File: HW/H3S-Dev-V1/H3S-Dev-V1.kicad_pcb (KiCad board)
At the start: 2 copper layers, 85 x 56 mm, 17 parts, among them J1 USB_C_Receptacle_USB2.0_16P, J2 Conn_01x02_Socket, J3 Conn_Coaxial, Q1 DMP3099L, U1 Ai-Thinker-Ra-01, U2 LTC4054ES5-4.2, U4 ESP32-S3-WROOM-1

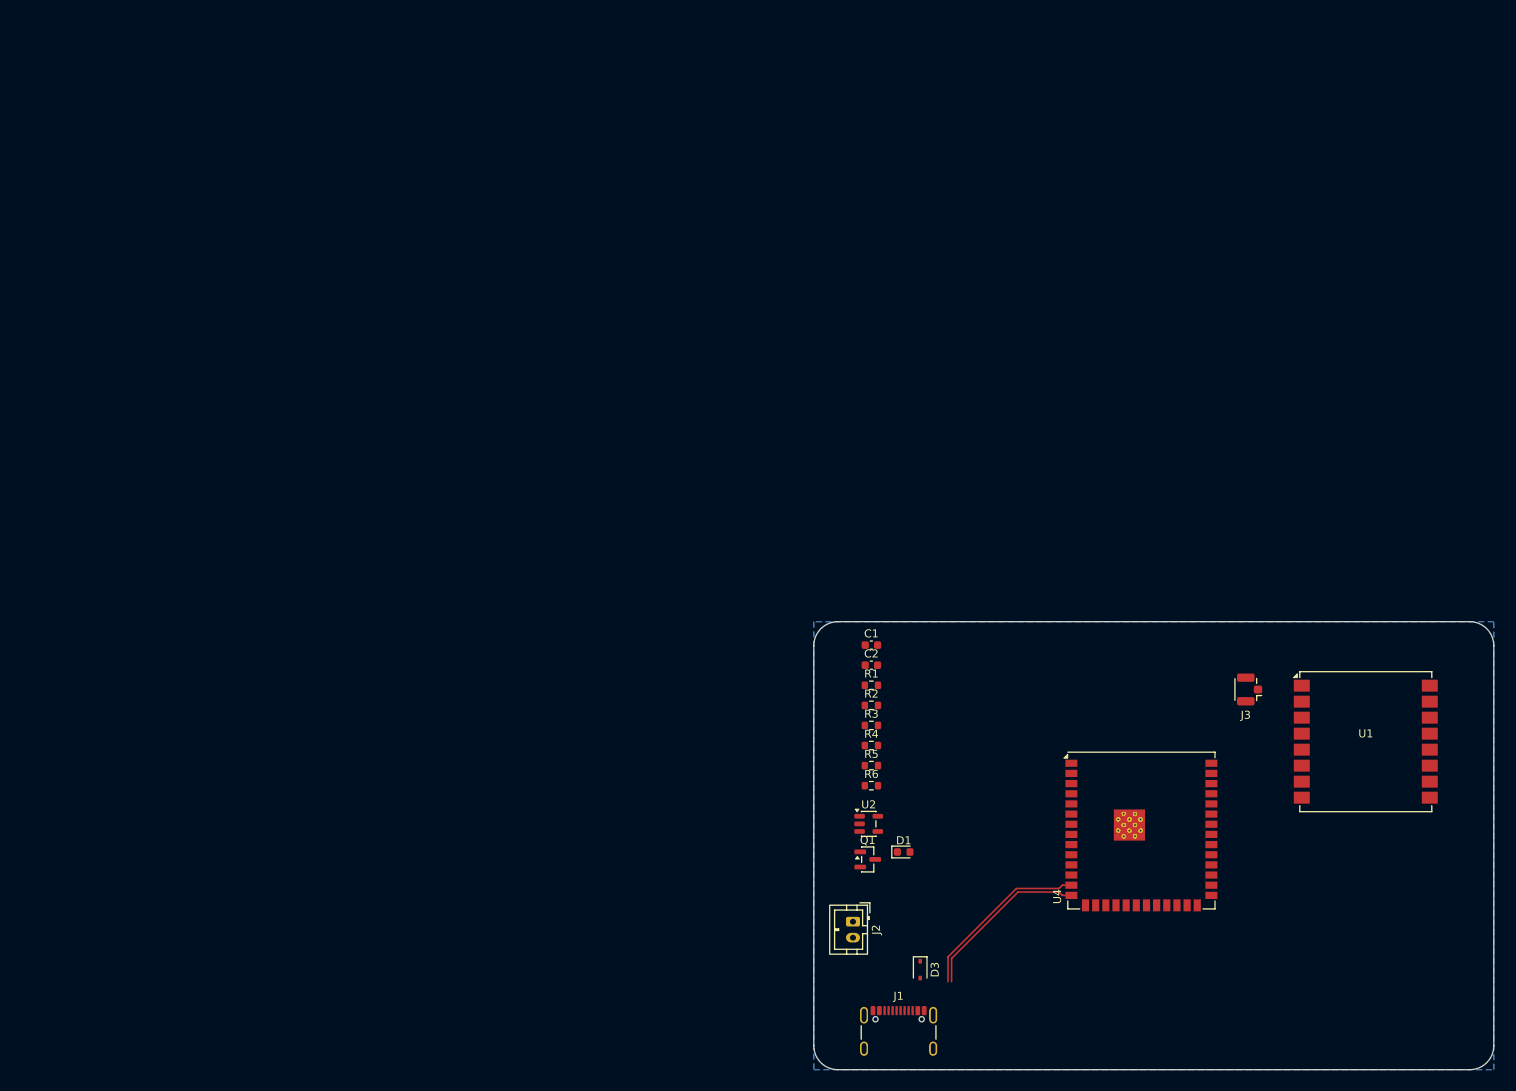
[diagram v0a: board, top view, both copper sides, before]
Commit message: Some components arranged
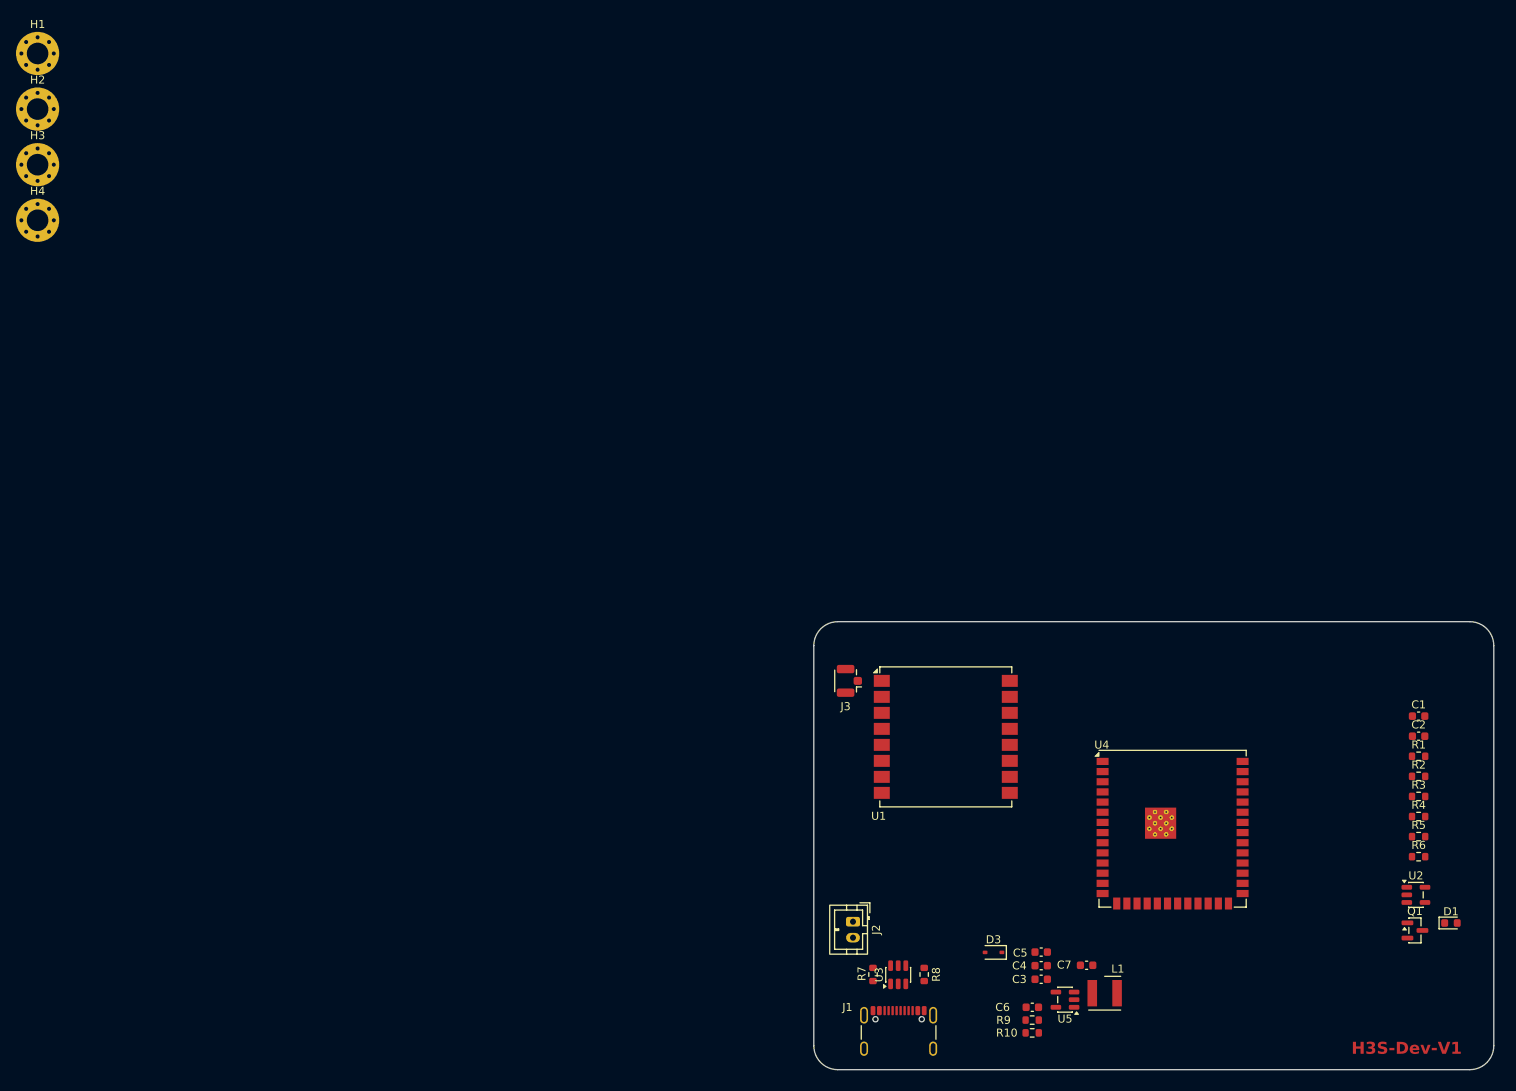
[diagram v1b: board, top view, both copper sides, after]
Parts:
- added C3: 100n, Capacitor_SMD:C_0603_1608Metric, F.Cu at (128.4, 118.7)
- added C4: 22u, Capacitor_SMD:C_0603_1608Metric, F.Cu at (128.4, 117.0)
- added C5: 22u, Capacitor_SMD:C_0603_1608Metric, F.Cu at (128.4, 115.3)
- added C6: 22p, Capacitor_SMD:C_0603_1608Metric, F.Cu at (127.3, 122.2)
- added C7: 22u, Capacitor_SMD:C_0603_1608Metric, F.Cu at (134.1, 117.0)
- added H1: MountingHole_Pad_MP, MountingHole:MountingHole_2.7mm_M2.5_Pad_Via, F.Cu at (2.98, 2.98)
- added H2: MountingHole_Pad_MP, MountingHole:MountingHole_2.7mm_M2.5_Pad_Via, F.Cu at (2.98, 9.93)
- added H3: MountingHole_Pad_MP, MountingHole:MountingHole_2.7mm_M2.5_Pad_Via, F.Cu at (2.98, 16.9)
- added H4: MountingHole_Pad_MP, MountingHole:MountingHole_2.7mm_M2.5_Pad_Via, F.Cu at (2.98, 23.8)
- added L1: 22uH, Inductor_SMD_Wurth:L_Wurth_WE-LQSH-4020, F.Cu at (136.4, 120.4)
- added R10: 49.9k/1%, Resistor_SMD:R_0603_1608Metric, F.Cu at (127.3, 125.4)
- added R7: 5.1k, Resistor_SMD:R_0603_1608Metric, F.Cu at (107.4, 118.1)
- added R8: 5.1k, Resistor_SMD:R_0603_1608Metric, F.Cu at (113.8, 118.1)
- added R9: 220k/1%, Resistor_SMD:R_0603_1608Metric, F.Cu at (127.3, 123.8)
- added U3: USBLC6-2SC6, Package_TO_SOT_SMD:SOT-23-6, F.Cu at (110.5, 118.1)
- added U5: SY8089AAAC, Package_TO_SOT_SMD:SOT-23-5, F.Cu at (131.4, 121.2)
- moved D1 69.0 mm to (179.6, 111.7)
- moved Q1 69.0 mm to (175.1, 112.6)
- moved C1 69.0 mm to (175.6, 85.8)
- moved C2 69.0 mm to (175.6, 88.3)
- moved R1 69.0 mm to (175.6, 90.8)
- moved R2 69.0 mm to (175.6, 93.3)
- moved R3 69.0 mm to (175.6, 95.8)
- moved R4 69.0 mm to (175.6, 98.4)
- moved R5 69.0 mm to (175.6, 100.9)
- moved R6 69.0 mm to (175.6, 103.4)
- moved U2 69.0 mm to (175.3, 108.2)
- moved U1 52.5 mm to (116.5, 88.4)
- moved J3 50.0 mm to (104.5, 81.4)
- moved D3 9.41 mm to (122.5, 115.3), turned to 180 degrees
- moved U4 3.91 mm to (144.8, 99.9)
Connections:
- net /VCC5 renamed /VBUS
- J1 pad A5: unconnected-(J1-CC1-PadA5) -> Net-(J1-CC1)
- J1 pad B5: unconnected-(J1-CC2-PadB5) -> Net-(J1-CC2)
- U1 pad 3: unconnected-(U1-VDD-Pad3) -> VCC
- U4 pad 13: /USB_D- -> Net-(U4-USB_D-)
- U4 pad 14: /USB_D+ -> Net-(U4-USB_D+)
- U4 pad 2: unconnected-(U4-3V3-Pad2) -> VCC
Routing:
- net /USB_D-: track 22.2 -> 0.00 mm
- net /USB_D+: track 21.5 -> 0.00 mm
- removed copper zone on B.Cu, net GND
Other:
- board text added: "H3S-Dev-V1"

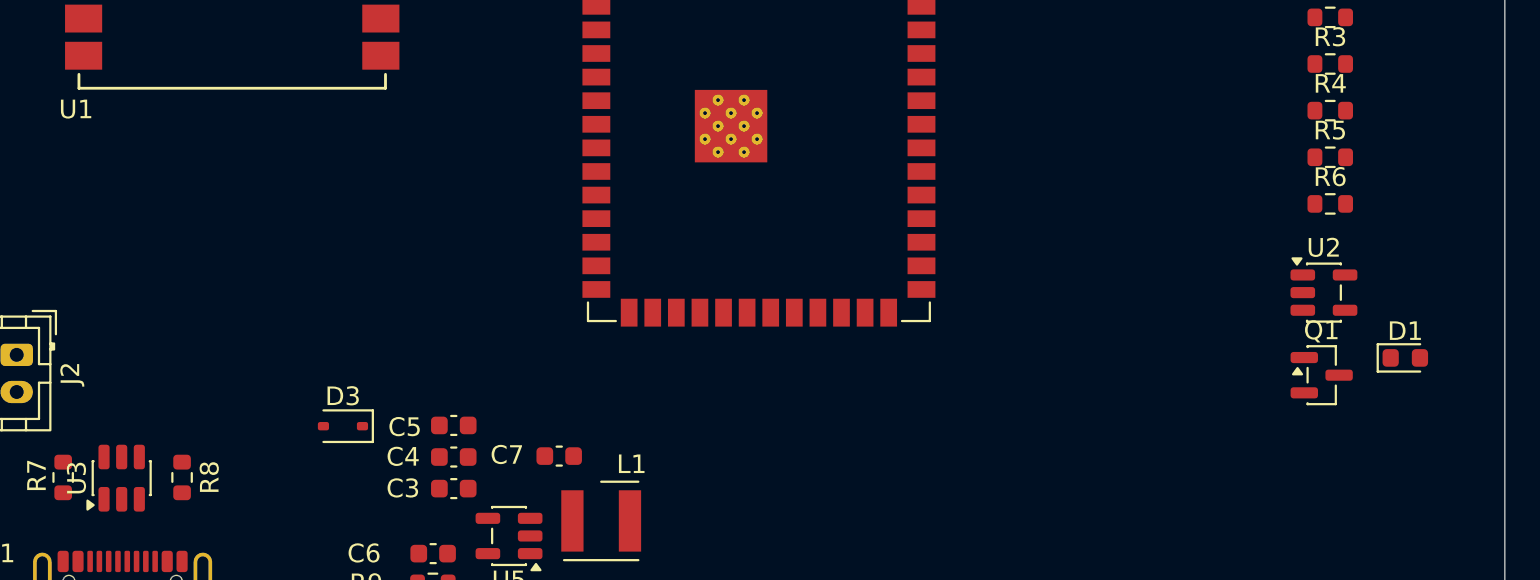
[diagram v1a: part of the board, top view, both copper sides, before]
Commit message: Charger works
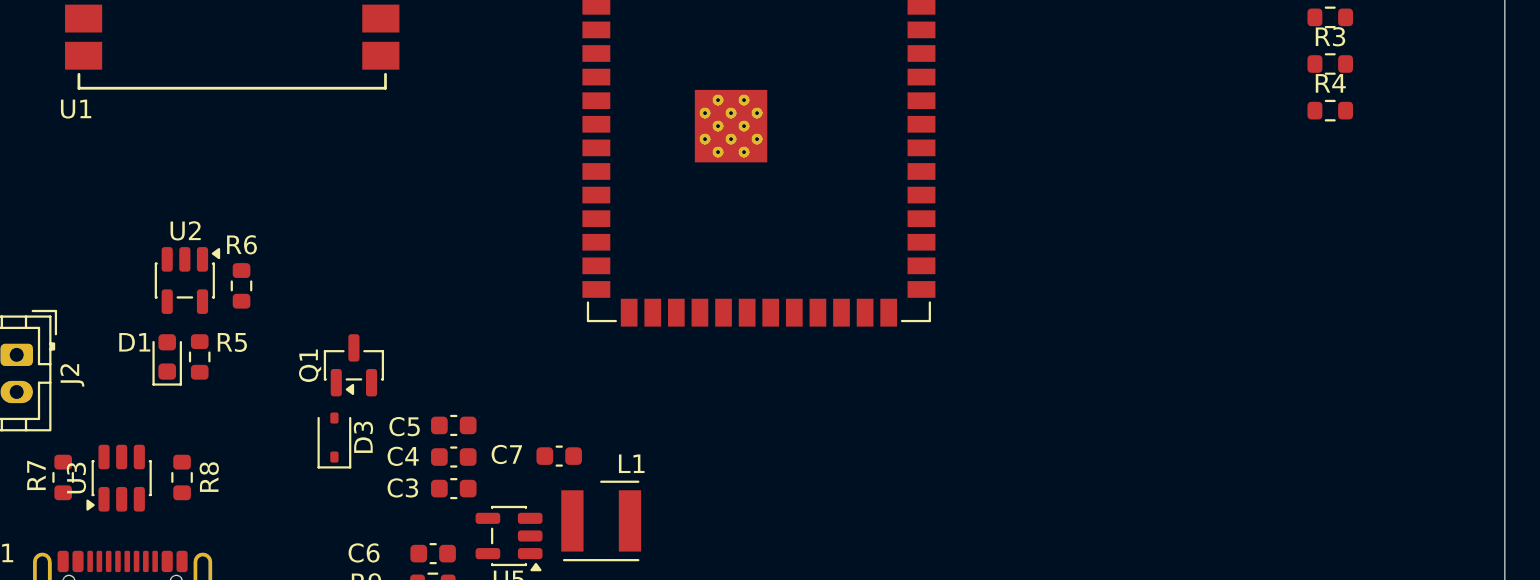
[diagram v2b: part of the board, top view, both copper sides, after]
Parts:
- moved D1 66.6 mm to (113.0, 111.6), turned to 90 degrees
- moved R5 61.8 mm to (114.8, 111.6), turned to 90 degrees
- moved U2 61.3 mm to (114.0, 107.5), turned to -90 degrees
- moved R6 58.8 mm to (117.0, 107.8), turned to 90 degrees
- moved Q1 52.1 mm to (123.0, 112.1), turned to 90 degrees
- moved D3 0.76 mm to (122.0, 116.0), turned to 90 degrees
